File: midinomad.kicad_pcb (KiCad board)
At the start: 2 copper layers, 43 parts, among them J1 DIN-5_180degree, J2 DIN-5_180degree, J3 DIN-8, SW1 SW_Push, SW2 SW_Push, SW3 SW_Push, SW4 SW_Push, SW5 SW_Push, SW6 SW_Push, U1 6N138

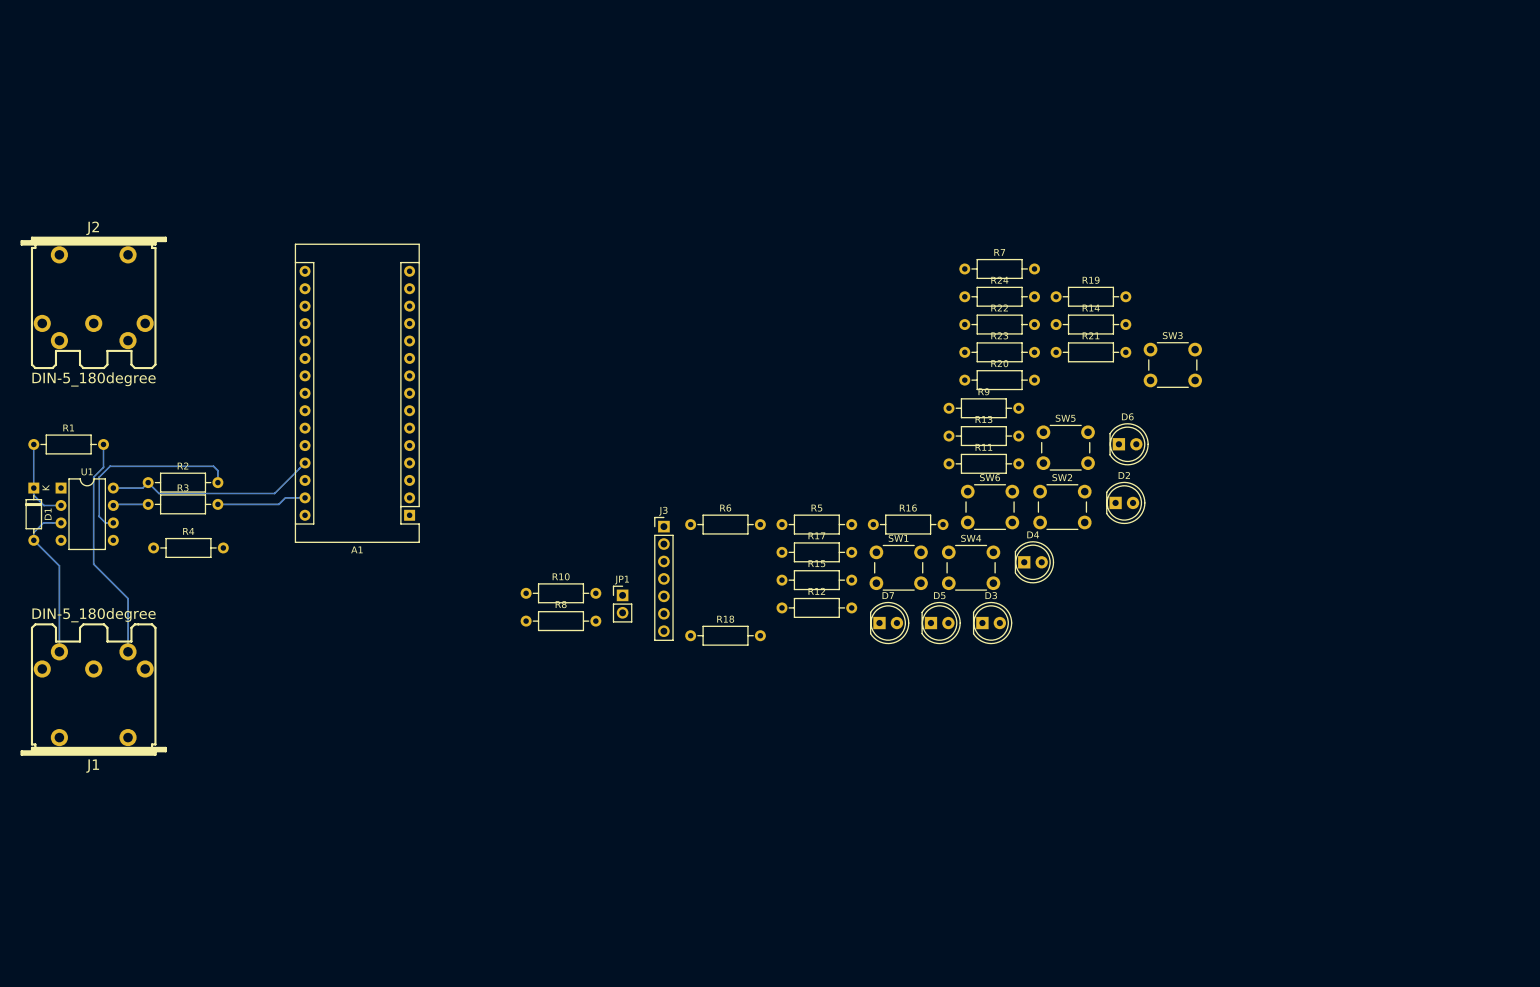
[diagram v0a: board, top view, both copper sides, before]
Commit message: schematics updated, using analog mux for vch switching, PCB nearly done
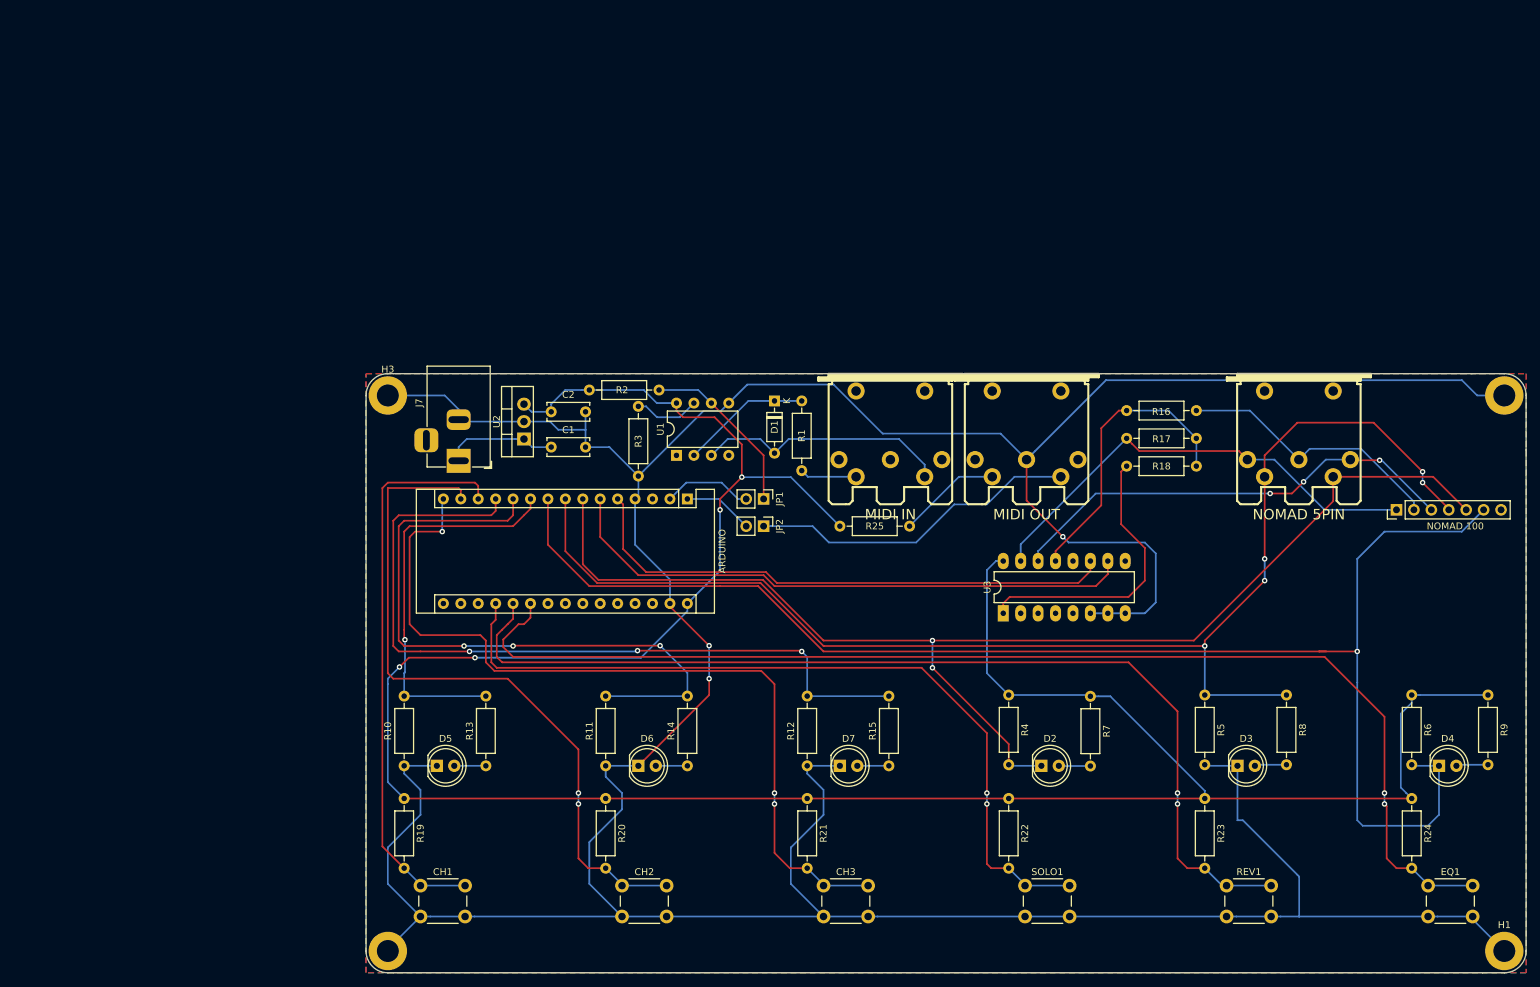
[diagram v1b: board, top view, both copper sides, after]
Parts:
- removed A1: Arduino_Nano_v3.x, Module:Arduino_Nano
- removed SW1, SW2, SW3, SW4, SW5, SW6: SW_Push, Button_Switch_THT:SW_PUSH_6mm
- added ARDUINO: Arduino_Nano_v3.x, Module:Arduino_Nano, F.Cu at (111.9, 91.3)
- added C1: 0.33uF, Capacitor_THT:C_Disc_D6.0mm_W2.5mm_P5.00mm, F.Cu at (92.1, 83.7)
- added C2: 0.1uF, Capacitor_THT:C_Disc_D6.0mm_W2.5mm_P5.00mm, F.Cu at (92.1, 78.6)
- added CH1: SW_Push, Button_Switch_THT:SW_PUSH_6mm, F.Cu at (73.0, 147.6)
- added CH2: SW_Push, Button_Switch_THT:SW_PUSH_6mm, F.Cu at (102.4, 147.6)
- added CH3: SW_Push, Button_Switch_THT:SW_PUSH_6mm, F.Cu at (131.8, 147.6)
- added EQ1: SW_Push, Button_Switch_THT:SW_PUSH_6mm, F.Cu at (219.9, 147.6)
- added H1: MountingHole_Pad, MountingHole:MountingHole_3.2mm_M3_DIN965_Pad, F.Cu at (231.0, 157.2)
- added H2: MountingHole_Pad, MountingHole:MountingHole_3.2mm_M3_DIN965_Pad, F.Cu at (68.3, 157.2)
- added H3: MountingHole_Pad, MountingHole:MountingHole_3.2mm_M3_DIN965_Pad, F.Cu at (68.3, 76.2)
- added H4: MountingHole_Pad, MountingHole:MountingHole_3.2mm_M3_DIN965_Pad, F.Cu at (231.0, 76.2)
- added J7: DC IN, Connector_BarrelJack:BarrelJack_Horizontal, F.Cu at (78.6, 85.7)
- added JP2: Jumper, Connector_PinHeader_2.54mm:PinHeader_1x02_P2.54mm_Vertical, F.Cu at (123.0, 95.2)
- added NOMAD 100: Nomad 100, Connector_PinHeader_2.54mm:PinHeader_1x07_P2.54mm_Vertical, F.Cu at (215.3, 92.9)
- added R25: 220R, Resistor_THT:R_Axial_DIN0207_L6.3mm_D2.5mm_P10.16mm_Horizontal, F.Cu at (134.1, 95.2)
- added REV1: SW_Push, Button_Switch_THT:SW_PUSH_6mm, F.Cu at (190.5, 147.6)
- added SOLO1: SW_Push, Button_Switch_THT:SW_PUSH_6mm, F.Cu at (161.1, 147.6)
- added U2: L7805, Package_TO_SOT_THT:TO-220-3_Vertical, F.Cu at (88.1, 82.5)
- added U3: 74HC4053, Package_DIP:DIP-16_W7.62mm_LongPads, F.Cu at (158.0, 108.0)
- J1: value DIN-5_180degree -> MIDI IN
- J2: value DIN-5_180degree -> MIDI OUT
- J3: value DIN-8 -> NOMAD 5PIN; footprint Connector_PinHeader_2.54mm:PinHeader_1x07_P2.54mm_Vertical -> w_conn_av:din-5
- moved J2 137.4 mm to (161.4, 82.5)
- moved R4 126.4 mm to (158.8, 119.9), turned to 270 degrees
- moved J1 121.7 mm to (141.5, 82.5), turned to 180 degrees
- moved R19 119.9 mm to (70.6, 134.9), turned to 270 degrees
- moved R1 112.1 mm to (128.6, 77.0), turned to 270 degrees
- moved R8 111.3 mm to (199.2, 119.9), turned to 270 degrees
- moved D1 108.7 mm to (124.6, 77.0)
- moved R6 108.0 mm to (217.5, 119.9), turned to 270 degrees
- moved R24 97.9 mm to (217.5, 134.9), turned to 270 degrees
- moved J3 93.4 mm to (201.0, 82.5), turned to 180 degrees
- moved U1 89.8 mm to (110.3, 84.9), turned to 90 degrees
- moved R9 89.0 mm to (228.6, 119.9), turned to 270 degrees
- moved D6 84.3 mm to (104.8, 130.2)
- moved R14 83.8 mm to (111.9, 130.2), turned to 90 degrees
- moved R13 82.9 mm to (82.5, 130.2), turned to 90 degrees
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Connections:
- J2 pad 1: -3V -> Net-(J2-Pad1)
- J2 pad 2: +2V -> GNDREF
- J2 pad 3: MESA_VCH -> Net-(J2-Pad3)
- J2 pad 4: Arduino_D5 -> Net-(J2-Pad4)
- J2 pad 5: Arduino_D4 -> Tx
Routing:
- net GNDREF: track 13.1 -> 578.0 mm, vias 0 -> 3
- net +5V: track 30.8 -> 382.2 mm, vias 0 -> 4
- net Arduino_D6: track 0.00 -> 215.6 mm, vias 0 -> 1
- net Arduino_D5: track 0.00 -> 192.1 mm, vias 0 -> 5
- net Arduino_D4: track 0.00 -> 184.4 mm, vias 0 -> 2
- net Arduino_A2: track 0.00 -> 176.1 mm, vias 0 -> 2
- net Arduino_A1: track 0.00 -> 148.0 mm, vias 0 -> 2
- net Arduino_D12: track 0.00 -> 121.6 mm, vias 0 -> 3
- net Arduino_A0: track 0.00 -> 117.9 mm, vias 0 -> 2
- net Arduino_D9: track 0.00 -> 114.9 mm, vias 0 -> 3
- net Arduino_D11: track 0.00 -> 101.9 mm, vias 0 -> 2
- net Arduino_D8: track 0.00 -> 95.7 mm, vias 0 -> 3
- net Arduino_D3: track 0.00 -> 85.1 mm
- net Arduino_D10: track 0.00 -> 83.1 mm
- net Arduino_D2: track 0.00 -> 80.0 mm
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- added copper zone on B.Cu, net GNDREF
- added copper zone on F.Cu, net GNDREF
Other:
- board outline added: 169.1 x 87.3 mm

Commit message: Rev 4 schematics, rev 3 pcb
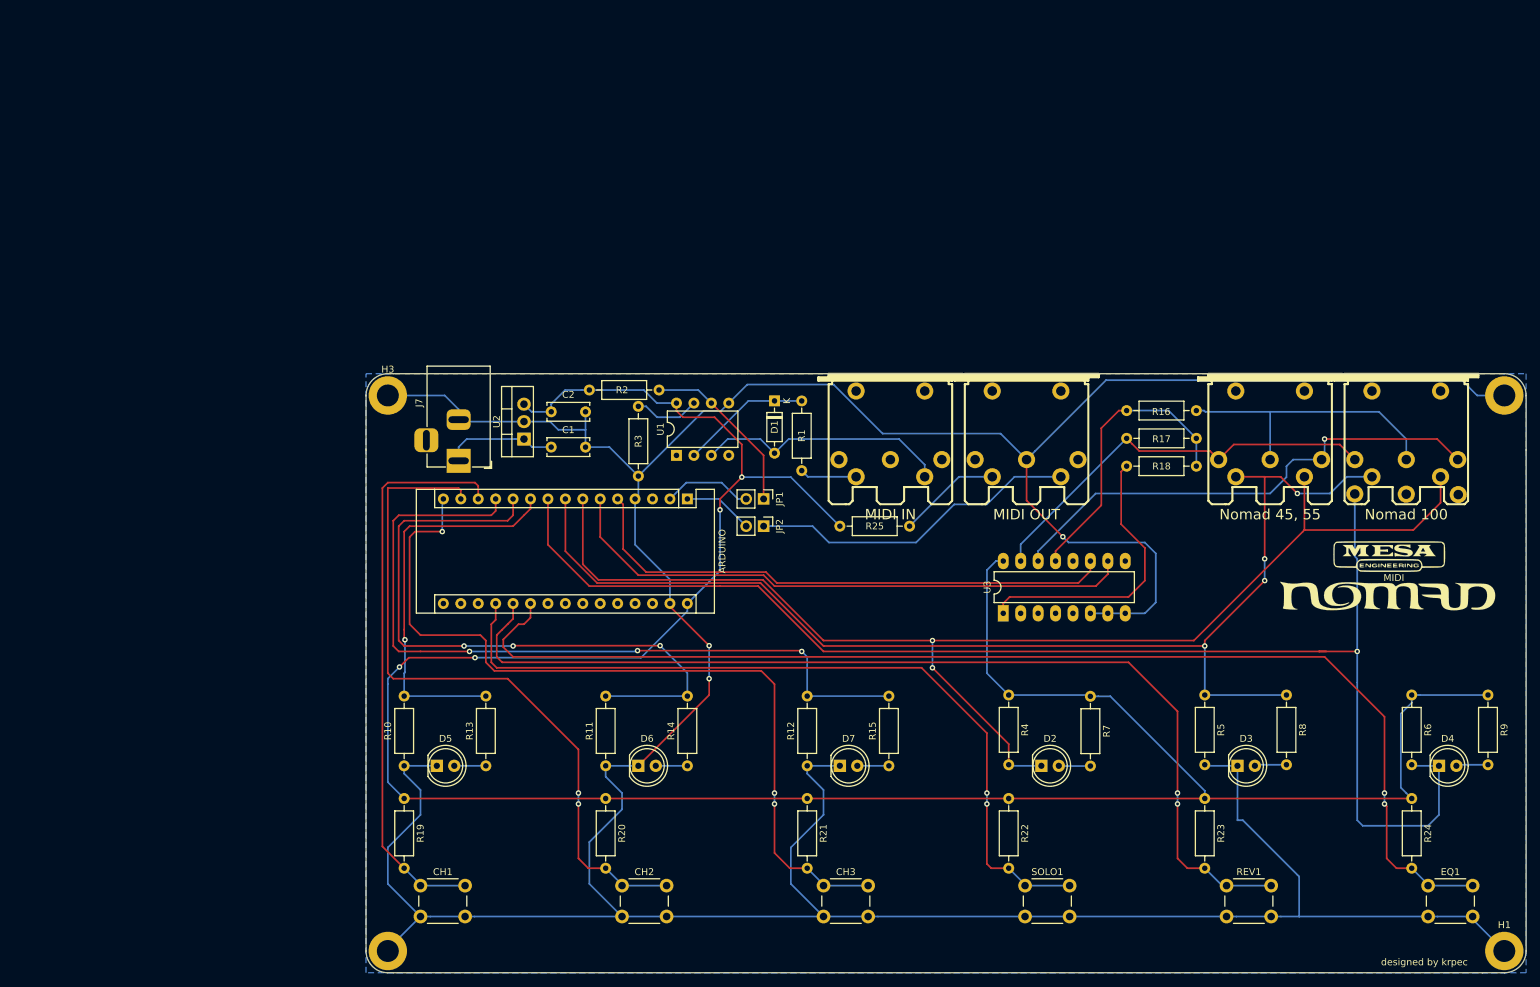
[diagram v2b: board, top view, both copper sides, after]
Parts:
- added G***: LOGO, midinomad-bl:board-logo, F.Cu at (214.3, 101.6)
- J3: value NOMAD 5PIN -> Nomad 45, 55
- NOMAD 100: footprint Connector_PinHeader_2.54mm:PinHeader_1x07_P2.54mm_Vertical -> midinomad:din-8
- moved NOMAD 100 10.4 mm to (216.7, 82.5), turned to 180 degrees
- moved J3 4.19 mm to (196.8, 82.5)
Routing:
- net Arduino_D5: track 192.1 -> 175.7 mm, vias 5 -> 4
- net Arduino_D6: track 215.6 -> 203.9 mm
- net -3V: track 67.9 -> 60.6 mm
- net MESA_VCH: track 67.3 -> 73.0 mm, vias 3 -> 1
- net +2V: track 39.7 -> 42.3 mm
- net Arduino_D4: track 184.4 -> 186.5 mm
- removed copper zone on F.Cu, net GNDREF
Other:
- board text added: "MIDI"
- board text added: "designed by krpec"

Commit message: forgot to f*$%ing save the changes..
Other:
- board text added: "MIDI Nomad footswitch board, rev. 3"
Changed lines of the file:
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@@
   (general
     (thickness 1.6)
-    (drawings 18)
+    (drawings 19)
     (tracks 477)
     (zones 0)
@@
   (page A4)
   (title_block
+    (title "MIDI Nomad")
     (date 2020-04-05)
+    (rev 3)
+    (company "krpec - dittrich.r@gmail.com")
+    (comment 1 Untested.)
+    (comment 4 "Schematics partially inspired by HappySwitch - happyswitch.it")
   )
   (layers
@@
     )
   )
-  (gr_text "designed by krpec" (at 219.329 158.78175) (layer F.SilkS)
+  (gr_text "MIDI Nomad footswitch board, rev. 3" (at 212.598 158.65475) (layer F.SilkS)
     (effects (font (size 1 1) (thickness 0.15)))
   )
+  (gr_text "designed by krpec" (at 78.613 158.65475) (layer F.SilkS)
+    (effects (font (size 1 1) (thickness 0.15)))
+  )

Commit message: PCB rev. 4
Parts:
- moved G*** 5.56 mm to (208.8, 101.6)
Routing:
- net Arduino_D6: track 203.9 -> 229.7 mm, vias 1 -> 2
- net Arduino_D4: track 186.5 -> 196.3 mm
- net Arduino_D5: track 175.7 -> 183.1 mm
- net Arduino_D7: track 57.4 -> 59.0 mm
- net Arduino_A2: track 176.1 -> 175.0 mm
- net +5V: track 382.2 -> 383.2 mm
- removed copper zone on B.Cu, net GNDREF
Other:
- board text added: "MIDI Nomad footswitch board, rev. 4"
- board text removed: "MIDI Nomad footswitch board, rev. 3"
